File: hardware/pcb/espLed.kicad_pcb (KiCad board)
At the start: 2 copper layers, 23 parts, among them J1 led_strip, J2 flashing, J3 power, Q1 IRF9310TRPBF, Q2 AO3400A, Q3 AO3400A, Q4 AO3400A, SW1 reset, SW2 flash, U1 AMS1117-3.3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

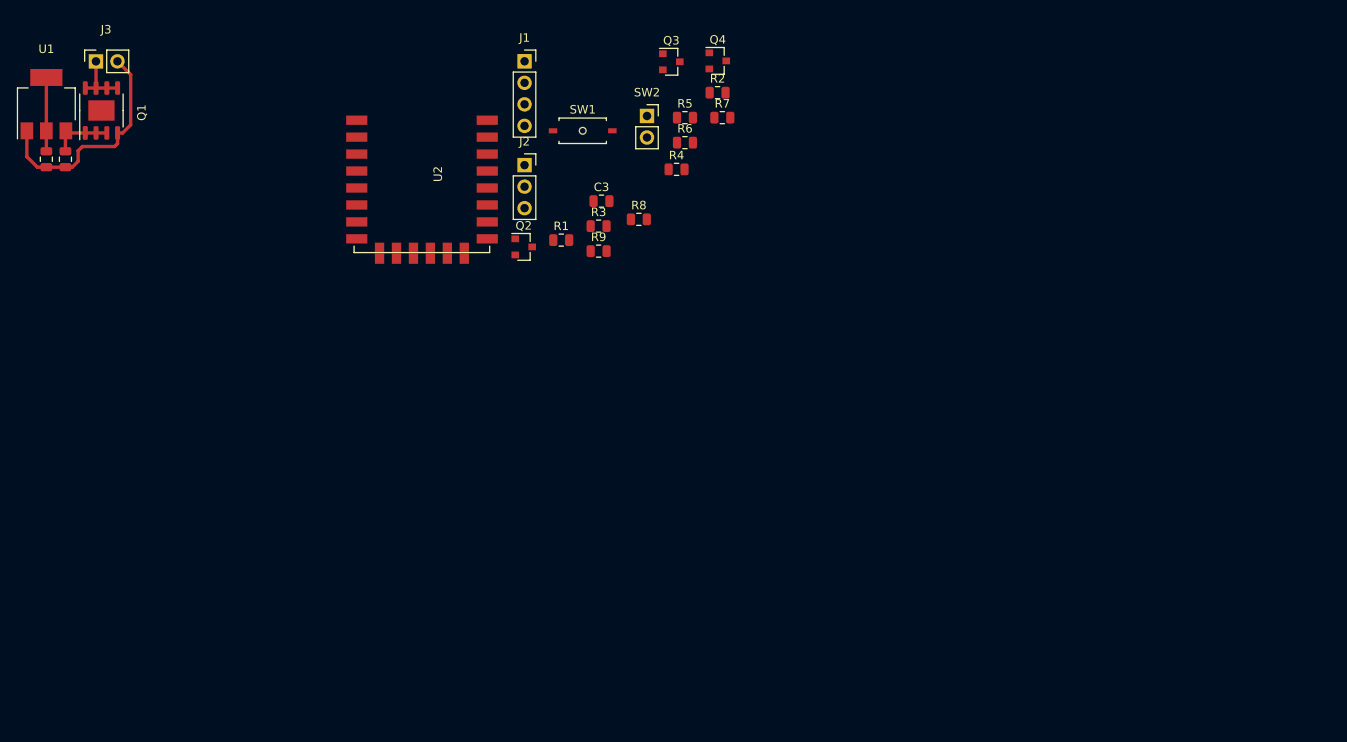
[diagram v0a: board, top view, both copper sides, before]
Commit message: layout circuitry for ESP
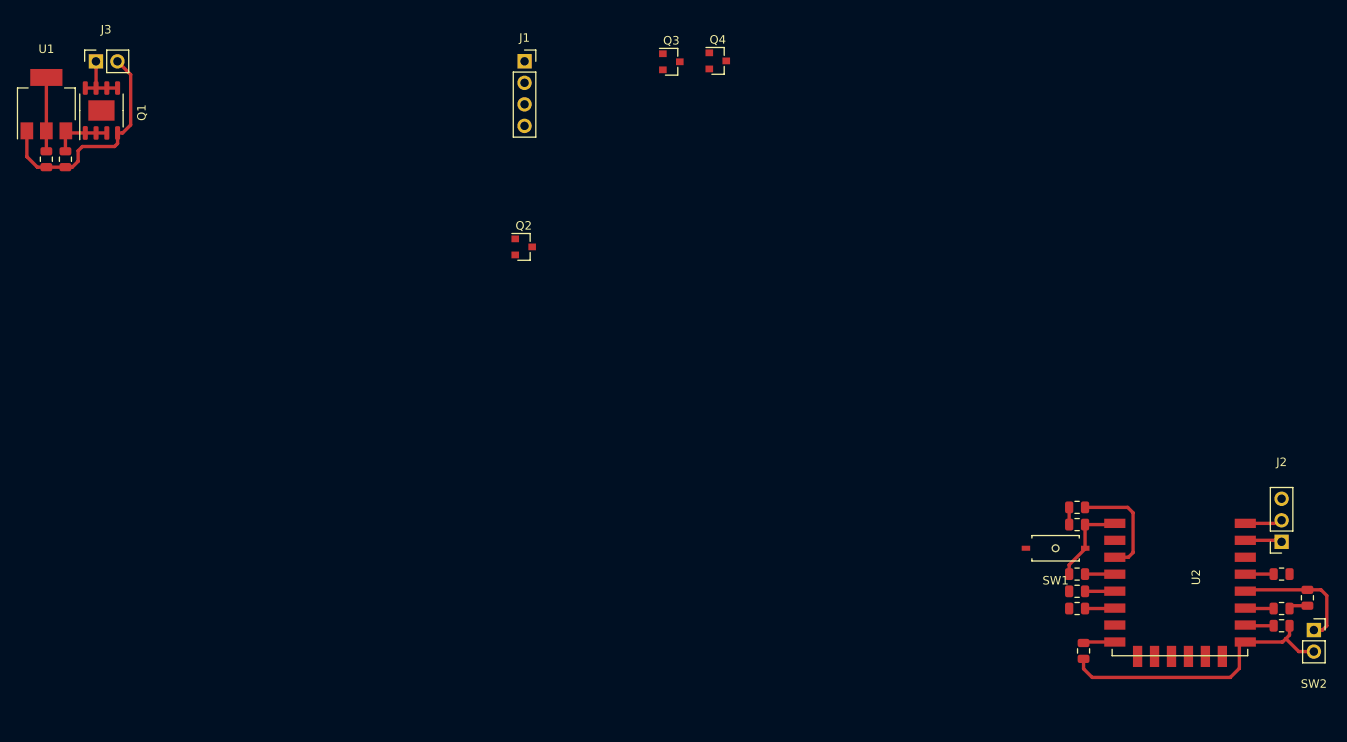
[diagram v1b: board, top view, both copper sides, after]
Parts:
- moved U2 101.3 mm to (172.3, 118.2)
- moved J2 99.8 mm to (191.3, 120.4), turned to 180 degrees
- moved SW2 99.4 mm to (195.1, 130.8)
- moved R9 91.9 mm to (191.3, 130.3), turned to 180 degrees
- moved R3 90.5 mm to (191.3, 124.2), turned to 180 degrees
- moved R7 89.3 mm to (194.3, 127.0), turned to 90 degrees
- moved R8 88.7 mm to (191.3, 128.3), turned to 180 degrees
- moved C3 77.8 mm to (167.9, 133.3), turned to 270 degrees
- moved SW1 74.4 mm to (164.6, 121.2)
- moved R2 74.2 mm to (167.1, 128.3)
- moved R1 73.6 mm to (167.1, 126.2)
- moved R5 71.0 mm to (167.1, 124.2), turned to 180 degrees
- moved R6 63.2 mm to (167.1, 116.3)
- moved R4 63.2 mm to (167.1, 118.4)
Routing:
- net GND: track 27.5 -> 62.3 mm
- net Net-(R7-Pad2): track 0.00 -> 16.0 mm
- net Net-(R6-Pad2): track 0.00 -> 12.4 mm
- net Net-(R4-Pad2): track 0.00 -> 11.2 mm
- net +3V3: track 8.71 -> 17.4 mm
- net /RX: track 0.00 -> 5.13 mm
- net /TX: track 0.00 -> 5.05 mm
- net /led2: track 0.00 -> 4.23 mm
- net /led1: track 0.00 -> 4.22 mm
- net Net-(R5-Pad1): track 0.00 -> 4.22 mm
- net Net-(R9-Pad2): track 0.00 -> 4.08 mm
- net Net-(R8-Pad2): track 0.00 -> 4.07 mm
- net /led3: track 0.00 -> 4.05 mm

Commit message: layout the 'led driver' part of the scheme
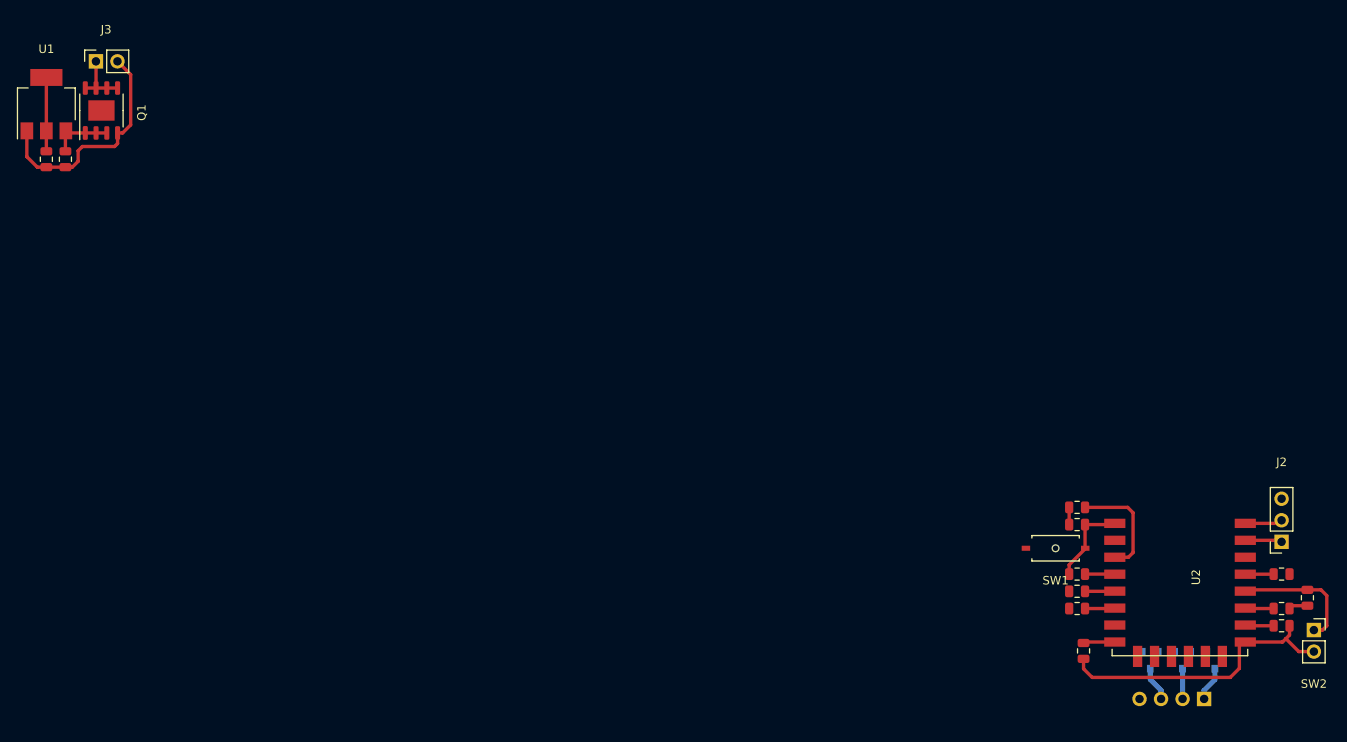
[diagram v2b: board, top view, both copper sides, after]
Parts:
- J1, Q2, Q3, Q4: moved to B.Cu
- moved J1 110.0 mm to (182.1, 138.9), turned to 90 degrees
- moved Q2 95.0 mm to (183.4, 134.4), turned to 270 degrees
- moved Q3 92.9 mm to (179.6, 134.4), turned to 270 degrees
- moved Q4 87.2 mm to (175.8, 134.4), turned to 270 degrees
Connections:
- R1 pad 1: Net-(Q2-Pad2) -> Net-(Q3-Pad2)
- R1 pad 2: /led1 -> /led2
- R2 pad 1: Net-(Q3-Pad2) -> Net-(Q4-Pad2)
- R2 pad 2: /led2 -> /led3
- R3 pad 1: Net-(Q4-Pad2) -> Net-(Q2-Pad2)
- R3 pad 2: /led3 -> /led1
- U2 pad 13: /led3 -> /led1
- U2 pad 5: /led1 -> /led2
- U2 pad 6: /led2 -> /led3
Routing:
- net /led3_out: track 0.00 -> 4.10 mm
- net /led1_out: track 0.00 -> 4.10 mm
- net /led2_out: track 0.00 -> 3.57 mm

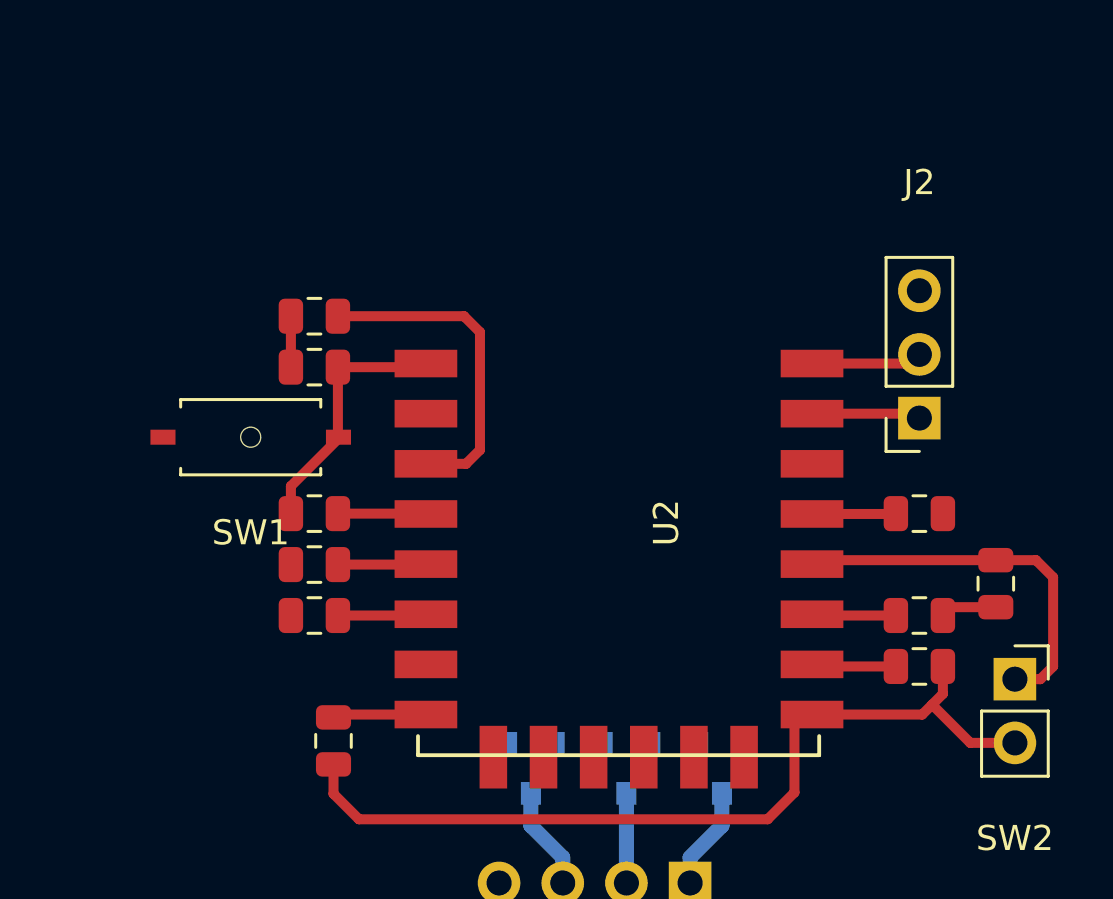
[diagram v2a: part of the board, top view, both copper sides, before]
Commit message: move the reset button and rearrange some components around it
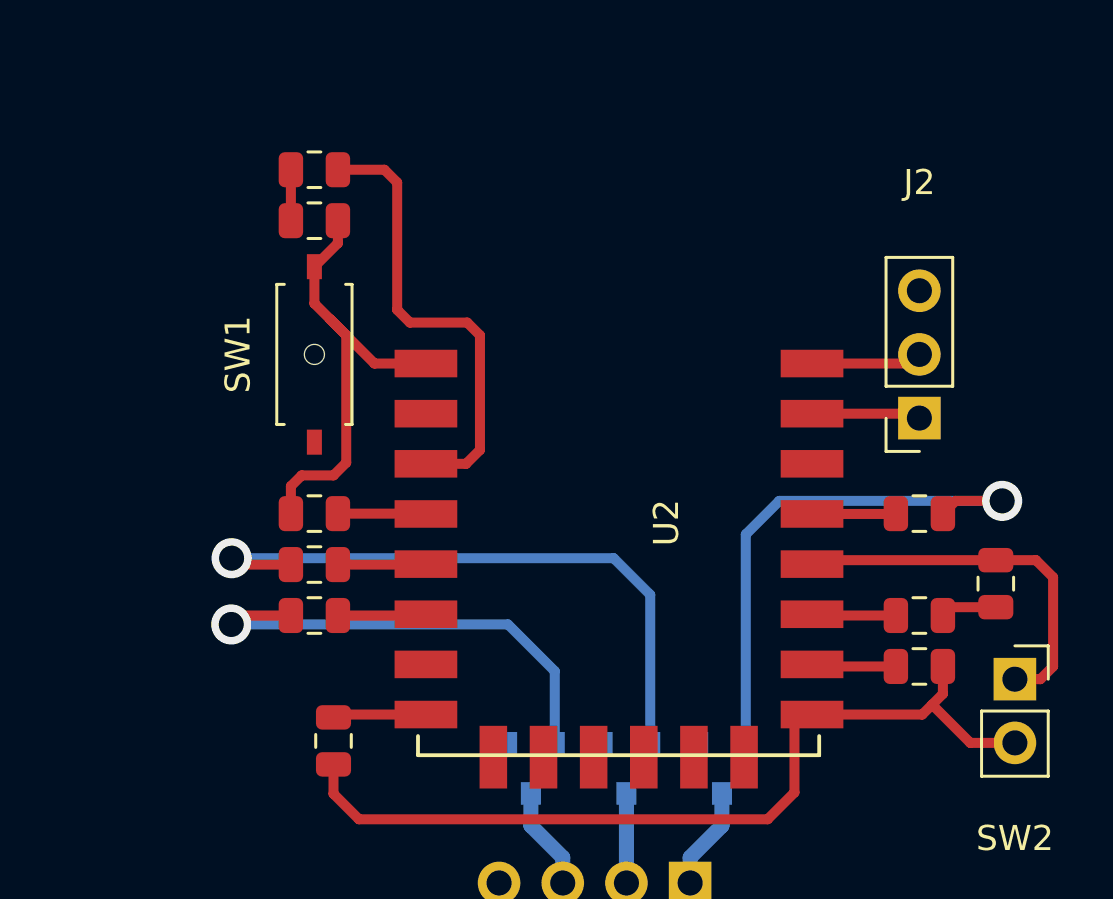
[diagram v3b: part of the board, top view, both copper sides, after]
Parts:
- moved R4 5.84 mm to (167.1, 112.5)
- moved R6 5.84 mm to (167.1, 110.5)
- moved SW1 4.17 mm to (167.1, 117.9), turned to 90 degrees
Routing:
- net Net-(Q3-Pad2): track 0.00 -> 25.7 mm, vias 0 -> 1
- net Net-(Q2-Pad2): track 0.00 -> 21.7 mm, vias 0 -> 1
- net Net-(Q4-Pad2): track 0.00 -> 19.1 mm, vias 0 -> 1
- net Net-(R4-Pad2): track 11.2 -> 20.0 mm
- net Net-(R6-Pad2): track 12.4 -> 17.7 mm
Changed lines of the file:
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@@
     (thickness 1.6)
     (drawings 0)
-    (tracks 87)
+    (tracks 115)
     (zones 0)
     (modules 23)
@@
   )
   (module custom:push_button (layer F.Cu)
-    (at 164.592 121.158)
+    (at 167.132 117.856 90)
     (descr "Ultra-small-sized Tactile Switch with High Contact Reliability, Top-actuated Model, without Ground Terminal, with Boss")
     (tags "Tactile Switch")
     (attr smd)
-    (fp_text reference SW1 (at 0 3.81) (layer F.SilkS)
-      (effects (font (size 1 1) (thickness 0.15)))
-    )
-    (fp_text value reset (at 0 2.5) (layer F.Fab)
+    (fp_text reference SW1 (at 0 -3.048 90) (layer F.SilkS)
+      (effects (font (size 1 1) (thickness 0.15)))
+    )
+    (fp_text value reset (at -0.254 -2.286 90) (layer F.Fab)
       (effects (font (size 1 1) (thickness 0.15)))
     )
@@
     (fp_line (start -2.54 1.25) (end -2.54 -1.25) (layer F.Fab) (width 0.1))
     (fp_circle (center 0 0) (end 0.75 0) (layer F.Fab) (width 0.1))
-    (fp_text user %R (at 0 -2.5) (layer F.Fab) hide
-      (effects (font (size 1 1) (thickness 0.15)))
-    )
-    (pad 2 smd rect (at 3.5 0) (size 1 0.6) (layers F.Cu F.Paste F.Mask)
+    (fp_text user %R (at 0 -2.5 90) (layer F.Fab) hide
+      (effects (font (size 1 1) (thickness 0.15)))
+    )
+    (pad 2 smd rect (at 3.5 0 90) (size 1 0.6) (layers F.Cu F.Paste F.Mask)
       (net 16 "Net-(R4-Pad2)"))
-    (pad "" np_thru_hole circle (at 0 0) (size 0.8 0.8) (drill 0.8) (layers *.Cu *.Mask))
-    (pad 1 smd rect (at -3.5 0) (size 1 0.6) (layers F.Cu F.Paste F.Mask)
+    (pad "" np_thru_hole circle (at 0 0 90) (size 0.8 0.8) (drill 0.8) (layers *.Cu *.Mask))
+    (pad 1 smd rect (at -3.5 0 90) (size 1 0.6) (layers F.Cu F.Paste F.Mask)
       (net 1 GND))
     (model ${KISYS3DMOD}/Button_Switch_SMD.3dshapes/SW_SPST_B3U-1000P-B.wrl
@@
   )
   (module Resistor_SMD:R_0805_2012Metric (layer F.Cu)
-    (at 167.132 116.332)
+    (at 167.132 110.49)
     (descr "Resistor SMD 0805 (2012 Metric), square (rectangular) end terminal, IPC_7351 nominal, (Body size source: https://docs.google.com/spreadsheets/d/1BsfQQcO9C6DZCsRaXUlFlo91Tg2WpOkGARC1WS5S8t0/edit?usp=sharing), generated with kicad-footprint-generator")
     (tags resistor)
@@
   )
   (module Resistor_SMD:R_0805_2012Metric (layer F.Cu)
-    (at 167.132 118.364)
+    (at 167.132 112.522)
     (descr "Resistor SMD 0805 (2012 Metric), square (rectangular) end terminal, IPC_7351 nominal, (Body size source: https://docs.google.com/spreadsheets/d/1BsfQQcO9C6DZCsRaXUlFlo91Tg2WpOkGARC1WS5S8t0/edit?usp=sharing), generated with kicad-footprint-generator")
     (tags resistor)
@@
   (segment (start 45.5 74.3125) (end 45.5 71.9) (width 0.4) (layer F.Cu) (net 3))
   (segment (start 45.5 71.9) (end 45.5 65.6) (width 0.4) (layer F.Cu) (net 3))
-  (segment (start 166.1945 116.332) (end 166.1945 118.364) (width 0.4) (layer F.Cu) (net 3))
   (segment (start 168.008 132.22) (end 167.894 132.334) (width 0.4) (layer F.Cu) (net 3))
   (segment (start 172.28 132.22) (end 168.008 132.22) (width 0.4) (layer F.Cu) (net 3))
   (segment (start 192.532 127.9375) (end 192.1995 128.27) (width 0.4) (layer F.Cu) (net 3))
   (segment (start 194.31 127.9375) (end 192.532 127.9375) (width 0.4) (layer F.Cu) (net 3))
+  (segment (start 166.1945 110.49) (end 166.1945 112.522) (width 0.4) (layer F.Cu) (net 3))
   (segment (start 175.768 136.652) (end 177.038 137.922) (width 0.6) (layer B.Cu) (net 4))
   (segment (start 177.038 137.922) (end 177.038 138.938) (width 0.6) (layer B.Cu) (net 4))
@@
   (segment (start 51.365 63.715) (end 51.35 63.7) (width 0.4) (layer F.Cu) (net 9))
   (segment (start 51.365 66.85) (end 51.365 63.715) (width 0.4) (layer F.Cu) (net 9))
+  (segment (start 184.338 133.366) (end 184.338 125.034) (width 0.4) (layer B.Cu) (net 10))
+  (via (at 194.564 123.698) (size 1.6) (drill 1) (layers F.Cu B.Cu) (net 10))
+  (segment (start 185.674 123.698) (end 194.564 123.698) (width 0.4) (layer B.Cu) (net 10))
+  (segment (start 184.338 125.034) (end 185.674 123.698) (width 0.4) (layer B.Cu) (net 10))
+  (segment (start 192.7075 123.698) (end 192.1995 124.206) (width 0.4) (layer F.Cu) (net 10))
+  (segment (start 194.564 123.698) (end 192.7075 123.698) (width 0.4) (layer F.Cu) (net 10))
+  (segment (start 179.07 125.984) (end 163.83 125.984) (width 0.4) (layer B.Cu) (net 11))
+  (segment (start 164.084 126.238) (end 163.83 125.984) (width 0.4) (layer F.Cu) (net 11))
+  (segment (start 166.1945 126.238) (end 164.084 126.238) (width 0.4) (layer F.Cu) (net 11))
+  (via (at 163.83 125.984) (size 1.6) (drill 1) (layers F.Cu B.Cu) (net 11))
+  (segment (start 180.528 133.366) (end 180.528 127.442) (width 0.4) (layer B.Cu) (net 11))
+  (segment (start 180.528 127.442) (end 179.07 125.984) (width 0.4) (layer B.Cu) (net 11))
+  (via (at 163.815298 128.626916) (size 1.6) (drill 1) (layers F.Cu B.Cu) (net 12))
+  (segment (start 176.718 133.366) (end 176.718 130.49) (width 0.4) (layer B.Cu) (net 12))
+  (segment (start 176.718 130.49) (end 174.854916 128.626916) (width 0.4) (layer B.Cu) (net 12))
+  (segment (start 174.854916 128.626916) (end 163.815298 128.626916) (width 0.4) (layer B.Cu) (net 12))
+  (segment (start 166.1945 128.27) (end 164.172214 128.27) (width 0.4) (layer F.Cu) (net 12))
+  (segment (start 164.172214 128.27) (end 163.815298 128.626916) (width 0.4) (layer F.Cu) (net 12))
   (segment (start 172.262 126.238) (end 172.28 126.22) (width 0.4) (layer F.Cu) (net 14))
   (segment (start 168.0695 126.238) (end 172.262 126.238) (width 0.4) (layer F.Cu) (net 14))
@@
   (segment (start 186.28 124.22) (end 190.3105 124.22) (width 0.4) (layer F.Cu) (net 13))
   (segment (start 172.136 118.364) (end 172.28 118.22) (width 0.4) (layer F.Cu) (net 16))
-  (segment (start 168.0695 118.364) (end 172.136 118.364) (width 0.4) (layer F.Cu) (net 16))
   (segment (start 165.9965 124.404) (end 166.1945 124.206) (width 0.4) (layer F.Cu) (net 16))
-  (segment (start 168.0695 121.1355) (end 168.092 121.158) (width 0.4) (layer F.Cu) (net 16))
-  (segment (start 168.0695 118.364) (end 168.0695 121.1355) (width 0.4) (layer F.Cu) (net 16))
-  (segment (start 166.1945 123.1115) (end 166.1945 124.206) (width 0.4) (layer F.Cu) (net 16))
-  (segment (start 168.092 121.214) (end 166.1945 123.1115) (width 0.4) (layer F.Cu) (net 16))
-  (segment (start 168.092 121.158) (end 168.092 121.214) (width 0.4) (layer F.Cu) (net 16))
+  (segment (start 166.1945 124.206) (end 166.1945 123.1115) (width 0.4) (layer F.Cu) (net 16))
+  (segment (start 166.1945 123.1115) (end 166.624 122.682) (width 0.4) (layer F.Cu) (net 16))
+  (segment (start 166.624 122.682) (end 167.894 122.682) (width 0.4) (layer F.Cu) (net 16))
+  (segment (start 172.28 118.22) (end 169.528 118.22) (width 0.4) (layer F.Cu) (net 16))
+  (segment (start 167.132 115.824) (end 167.132 114.356) (width 0.4) (layer F.Cu) (net 16))
+  (segment (start 168.0695 113.4185) (end 167.132 114.356) (width 0.4) (layer F.Cu) (net 16))
+  (segment (start 168.0695 112.522) (end 168.0695 113.4185) (width 0.4) (layer F.Cu) (net 16))
+  (segment (start 167.894 122.682) (end 168.402 122.174) (width 0.4) (layer F.Cu) (net 16))
+  (segment (start 168.402 117.094) (end 167.767 116.459) (width 0.4) (layer F.Cu) (net 16))
+  (segment (start 168.402 122.174) (end 168.402 117.094) (width 0.4) (layer F.Cu) (net 16))
+  (segment (start 167.767 116.459) (end 167.132 115.824) (width 0.4) (layer F.Cu) (net 16))
+  (segment (start 169.528 118.22) (end 167.767 116.459) (width 0.4) (layer F.Cu) (net 16))
   (segment (start 172.266 124.206) (end 172.28 124.22) (width 0.4) (layer F.Cu) (net 17))
   (segment (start 168.0695 124.206) (end 172.266 124.206) (width 0.4) (layer F.Cu) (net 17))
   (segment (start 172.234 122.174) (end 172.28 122.22) (width 0.4) (layer F.Cu) (net 18))
-  (segment (start 173.736 116.967) (end 173.101 116.332) (width 0.4) (layer F.Cu) (net 18))
-  (segment (start 173.736 121.666) (end 173.736 116.967) (width 0.4) (layer F.Cu) (net 18))
-  (segment (start 173.101 116.332) (end 168.0695 116.332) (width 0.4) (layer F.Cu) (net 18))
+  (segment (start 169.926 110.49) (end 168.0695 110.49) (width 0.4) (layer F.Cu) (net 18))
+  (segment (start 170.434 110.998) (end 169.926 110.49) (width 0.4) (layer F.Cu) (net 18))
+  (segment (start 170.434 116.078) (end 170.434 110.998) (width 0.4) (layer F.Cu) (net 18))
+  (segment (start 173.736 117.094) (end 173.228 116.586) (width 0.4) (layer F.Cu) (net 18))
+  (segment (start 173.736 121.666) (end 173.736 117.094) (width 0.4) (layer F.Cu) (net 18))
+  (segment (start 173.228 116.586) (end 170.942 116.586) (width 0.4) (layer F.Cu) (net 18))
   (segment (start 173.182 122.22) (end 173.736 121.666) (width 0.4) (layer F.Cu) (net 18))
+  (segment (start 170.942 116.586) (end 170.434 116.078) (width 0.4) (layer F.Cu) (net 18))
   (segment (start 172.28 122.22) (end 173.182 122.22) (width 0.4) (layer F.Cu) (net 18))
   (segment (start 186.28 126.22) (end 186.298 126.238) (width 0.4) (layer F.Cu) (net 19))
